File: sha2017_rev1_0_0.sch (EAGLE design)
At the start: 201 parts, among them IC1 CP210X_USB_UART, IC2 AP7215, IC3 ESP32WROOM32, IC4 TP4056, M1 MOTOR10MM, Q1 MMBT2222A, Q2 MMBT2222A, Q3 MMBT2222A, Q4 MMBT2222A, Q5 SI1304 BDL, Q6 MMBT2222A, T1 MOSFET-PCHANNEL, T2 MOSFET-PCHANNEL, T3 MOSFET-PCHANNEL, U1 MPR121QR2, X2 2908-05WB-MG, X4 JST-PH3

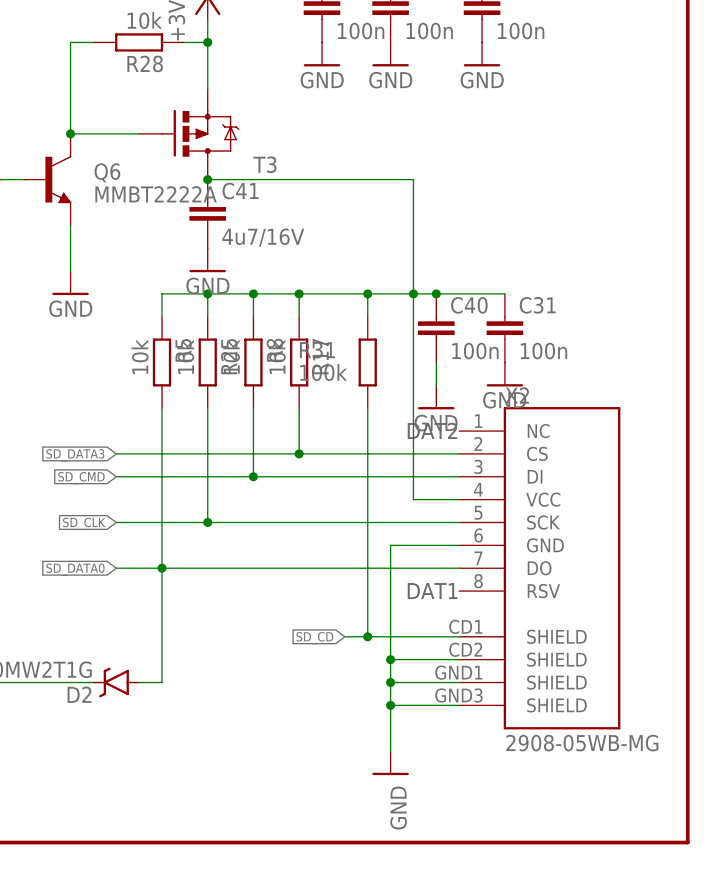
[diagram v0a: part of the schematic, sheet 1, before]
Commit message: Reverted power switches, re-routed touch controller
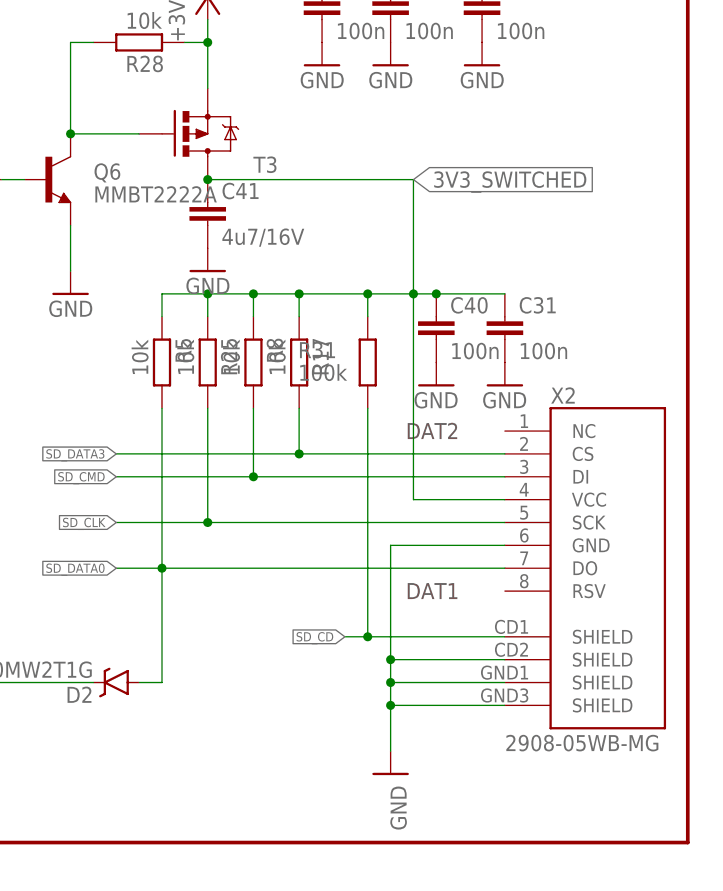
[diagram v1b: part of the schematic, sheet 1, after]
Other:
- moved on the sheet: X2
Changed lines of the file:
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@@
 </instance>
 <instance part="+3V10" gate="G$1" x="176.53" y="191.77" rot="R90"/>
-<instance part="X2" gate="G$1" x="363.22" y="76.2">
-<attribute name="PARTNO" x="363.22" y="76.2" size="1.778" layer="96" rot="MR0" display="off"/>
+<instance part="X2" gate="G$1" x="368.3" y="76.2" smashed="yes">
+<attribute name="PARTNO" x="368.3" y="76.2" size="1.778" layer="96" rot="MR0" display="off"/>
+<attribute name="NAME" x="365.76" y="91.948" size="1.778" layer="95"/>
+<attribute name="VALUE" x="360.68" y="53.34" size="1.778" layer="96"/>
 </instance>
 <instance part="GND59" gate="1" x="347.98" y="50.8" smashed="yes">
@@
 <attribute name="PARTNO" x="353.06" y="100.33" size="1.778" layer="96" rot="MR0" display="off"/>
 </instance>
-<instance part="GND17" gate="1" x="353.06" y="91.44"/>
+<instance part="GND17" gate="1" x="353.06" y="93.98"/>
 <instance part="FD4" gate="G$1" x="45.72" y="10.16">
 <attribute name="OC_FARNELL" x="45.72" y="10.16" size="1.778" layer="96" rot="MR0" display="off"/>
@@
 <segment>
 <pinref part="X2" gate="G$1" pin="SHIELD@4"/>
-<wire x1="355.6" y1="58.42" x2="347.98" y2="58.42" width="0.1524" layer="91"/>
+<wire x1="360.68" y1="58.42" x2="347.98" y2="58.42" width="0.1524" layer="91"/>
 <pinref part="X2" gate="G$1" pin="SHIELD@3"/>
-<wire x1="355.6" y1="60.96" x2="347.98" y2="60.96" width="0.1524" layer="91"/>
+<wire x1="360.68" y1="60.96" x2="347.98" y2="60.96" width="0.1524" layer="91"/>
 <wire x1="347.98" y1="60.96" x2="347.98" y2="58.42" width="0.1524" layer="91"/>
 <pinref part="GND59" gate="1" pin="GND"/>
@@
 <junction x="347.98" y="58.42"/>
 <pinref part="X2" gate="G$1" pin="SHIELD@2"/>
-<wire x1="355.6" y1="63.5" x2="347.98" y2="63.5" width="0.1524" layer="91"/>
+<wire x1="360.68" y1="63.5" x2="347.98" y2="63.5" width="0.1524" layer="91"/>
 <wire x1="347.98" y1="63.5" x2="347.98" y2="60.96" width="0.1524" layer="91"/>
 <junction x="347.98" y="60.96"/>
 <pinref part="X2" gate="G$1" pin="GND"/>
-<wire x1="355.6" y1="76.2" x2="347.98" y2="76.2" width="0.1524" layer="91"/>
+<wire x1="360.68" y1="76.2" x2="347.98" y2="76.2" width="0.1524" layer="91"/>
 <wire x1="347.98" y1="76.2" x2="347.98" y2="63.5" width="0.1524" layer="91"/>
 <junction x="347.98" y="63.5"/>
@@
 <pinref part="C40" gate="G$1" pin="2"/>
 <pinref part="GND17" gate="1" pin="GND"/>
-<wire x1="353.06" y1="93.98" x2="353.06" y2="96.52" width="0.1524" layer="91"/>
 </segment>
 <segment>
@@
 <segment>
 <pinref part="X2" gate="G$1" pin="SCK"/>
-<wire x1="355.6" y1="78.74" x2="327.66" y2="78.74" width="0.1524" layer="91"/>
+<wire x1="360.68" y1="78.74" x2="327.66" y2="78.74" width="0.1524" layer="91"/>
 <label x="317.5" y="78.74" size="1.016" layer="95" rot="R180" xref="yes"/>
 <pinref part="R25" gate="G$1" pin="1"/>
@@
 <segment>
 <pinref part="X2" gate="G$1" pin="DI"/>
-<wire x1="355.6" y1="83.82" x2="332.74" y2="83.82" width="0.1524" layer="91"/>
+<wire x1="360.68" y1="83.82" x2="332.74" y2="83.82" width="0.1524" layer="91"/>
 <label x="317.5" y="83.82" size="1.016" layer="95" rot="R180" xref="yes"/>
 <pinref part="R8" gate="G$1" pin="1"/>
@@
 <segment>
 <pinref part="X2" gate="G$1" pin="SHIELD@1"/>
-<wire x1="355.6" y1="66.04" x2="345.44" y2="66.04" width="0.1524" layer="91"/>
+<wire x1="360.68" y1="66.04" x2="345.44" y2="66.04" width="0.1524" layer="91"/>
 <label x="342.9" y="66.04" size="1.016" layer="95" rot="R180" xref="yes"/>
 <pinref part="R31" gate="G$1" pin="2"/>
@@
 <wire x1="317.5" y1="73.66" x2="322.58" y2="73.66" width="0.1524" layer="91"/>
 <pinref part="X2" gate="G$1" pin="DO"/>
-<wire x1="355.6" y1="73.66" x2="322.58" y2="73.66" width="0.1524" layer="91"/>
+<wire x1="360.68" y1="73.66" x2="322.58" y2="73.66" width="0.1524" layer="91"/>
 </segment>
 <segment>
@@
 <segment>
 <pinref part="X2" gate="G$1" pin="CS"/>
-<wire x1="355.6" y1="86.36" x2="337.82" y2="86.36" width="0.1524" layer="91"/>
+<wire x1="360.68" y1="86.36" x2="337.82" y2="86.36" width="0.1524" layer="91"/>
 <label x="317.5" y="86.36" size="1.016" layer="95" rot="R180" xref="yes"/>
 <pinref part="R17" gate="G$1" pin="1"/>
@@
 <pinref part="X2" gate="G$1" pin="VCC"/>
 <wire x1="350.52" y1="104.14" x2="350.52" y2="81.28" width="0.1524" layer="91"/>
-<wire x1="350.52" y1="81.28" x2="355.6" y2="81.28" width="0.1524" layer="91"/>
+<wire x1="350.52" y1="81.28" x2="360.68" y2="81.28" width="0.1524" layer="91"/>
 <pinref part="C40" gate="G$1" pin="1"/>
 <wire x1="350.52" y1="104.14" x2="353.06" y2="104.14" width="0.1524" layer="91"/>
@@
 <wire x1="353.06" y1="104.14" x2="360.68" y2="104.14" width="0.1524" layer="91"/>
 <junction x="353.06" y="104.14"/>
+<label x="350.52" y="116.84" size="1.778" layer="95" xref="yes"/>
 </segment>
 <segment>
@@
 </segment>
 </net>
-<net name="N$1" class="0">
+<net name="N$1" class="3">
 <segment>
 <pinref part="TOUCH_A" gate="G$1" pin="P$1"/>
@@
 </segment>
 </net>
-<net name="N$6" class="0">
+<net name="N$6" class="3">
 <segment>
 <pinref part="U1" gate="A" pin="ELE11"/>
@@
 </segment>
 </net>
-<net name="N$46" class="0">
+<net name="N$46" class="3">
 <segment>
 <pinref part="U1" gate="A" pin="ELE10"/>
@@
 </segment>
 </net>
-<net name="N$24" class="0">
+<net name="N$24" class="3">
 <segment>
 <pinref part="U1" gate="A" pin="ELE9"/>
